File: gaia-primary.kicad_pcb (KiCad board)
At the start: 6 copper layers, 50 x 50 mm, 66 parts, among them IC2 ADXL375BCCZ, J1 Debug Connectors, J2 Conn_02x10_Odd_Even, J3 Conn_02x10_Odd_Even, Q1 BSS138, Q2 BSS138, U10 AP2112K-1.8, U11 AP2112K-3.3, U12 ICM-20948, U13 ICM-20948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

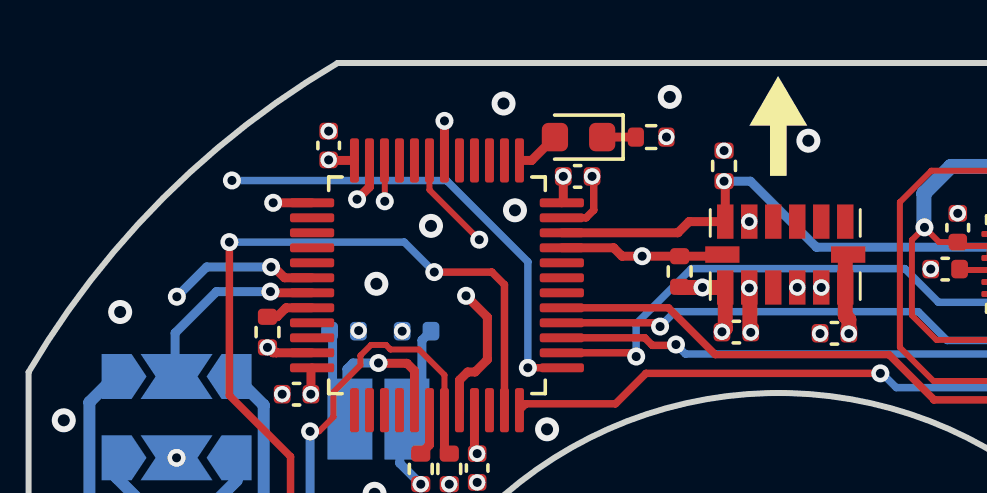
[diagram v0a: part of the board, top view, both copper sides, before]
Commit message: adding orientation star
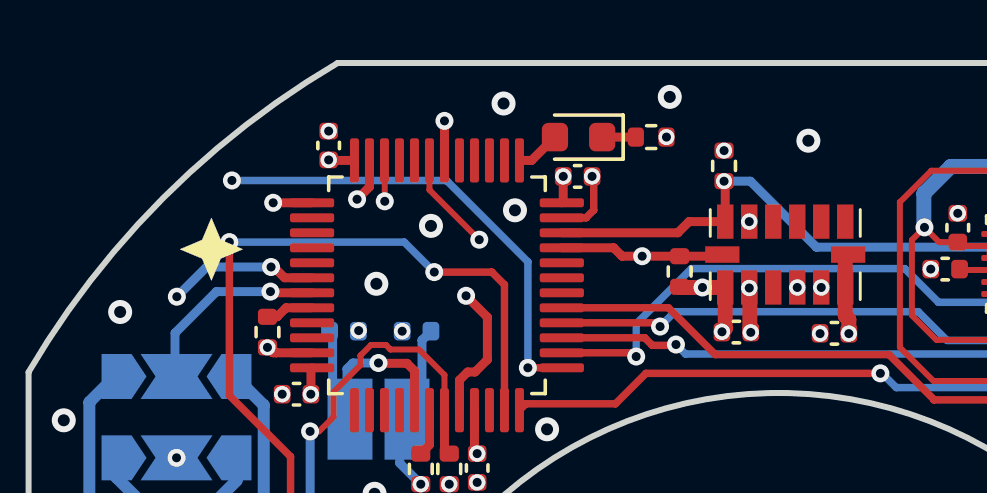
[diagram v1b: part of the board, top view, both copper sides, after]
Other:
- board text added: "revision 1.1"
- board text removed: "revision 1.1 Designed by Tamás Pécsi"
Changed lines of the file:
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@@
 	(gr_poly
 		(pts
-			(xy 189.180481 66.931062) (xy 190.156793 68.59) (xy 189.466231 68.59) (xy 189.466231 70.264812) (xy 188.910606 70.264812)
-			(xy 188.910606 68.59) (xy 188.220043 68.59)
+			(xy 170.6 72.4) (xy 171.329887 72.708337) (xy 170.6 73.016674) (xy 170.291663 73.746562) (xy 169.983325 73.016674)
+			(xy 169.253438 72.708337) (xy 169.983325 72.4) (xy 170.291663 71.670112)
 		)
 		(stroke
-			(width 0)
+			(width 0.017999)
 			(type solid)
+			(color 0 0 2 1)
 		)
 		(fill yes)
@@
 	(gr_poly
 		(pts
+			(xy 170.6 73) (xy 171.329887 72.691663) (xy 170.6 72.383326) (xy 170.291663 71.653438) (xy 169.983325 72.383326)
+			(xy 169.253438 72.691663) (xy 169.983325 73) (xy 170.291663 73.729888)
+		)
+		(stroke
+			(width 0.017999)
+			(type solid)
+			(color 0 0 2 1)
+		)
+		(fill yes)
+		(layer "B.SilkS")
+	)
+	(gr_poly
+		(pts
 			(xy 193.302391 110.900264) (xy 193.302391 111.73) (xy 193.559214 111.73) (xy 193.559214 110.529849)
 		)
@@
 		(layer "B.SilkS")
 	)
-	(gr_poly
-		(pts
-			(xy 189.196355 66.931062) (xy 188.220043 68.59) (xy 188.910605 68.59) (xy 188.910605 70.264812) (xy 189.46623 70.264812)
-			(xy 189.46623 68.59) (xy 190.156793 68.59)
-		)
-		(stroke
-			(width 0)
-			(type solid)
-		)
-		(fill yes)
-		(layer "B.SilkS")
-	)
 	(gr_arc
 		(start 214.196938 106.196938)
@@
 		)
 	)
-	(gr_text "revision 1.1\nDesigned by Tamás Pécsi"
+	(gr_text "revision 1.1"
 		(at 189.196938 114.752713 0)
 		(layer "B.SilkS")
@@
 	)
 	(group ""
-		(members "0d0d8099-fea4-4489-8b91-3eccab06b4e6")
+		(members "038ff78d-d753-476f-999a-6e016942f4b6")
 	)
 	(group ""
@@
 	)
 	(group ""
-		(members "f2d32b10-3288-46af-ae44-cc76b7697f8c")
+		(members "54acbaf3-46d5-42e8-81e1-9d1b1f8eff37")
 	)
 	(group ""
